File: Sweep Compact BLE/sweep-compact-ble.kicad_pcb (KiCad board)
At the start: 2 copper layers, 108.1 x 86.7 mm, 20 parts, among them SW10 SW_PUSH, SW11 SW_PUSH, SW12 SW_PUSH, SW14 SW_PUSH, SW15 SW_PUSH, SW16 SW_PUSH, SW17 SW_PUSH, SW18 SW_PUSH, SW2 SW_PUSH, SW20 SW_PUSH, SW21 SW_PUSH, SW3 SW_PUSH, SW4 SW_PUSH, SW5 SW_PUSH, SW6 SW_PUSH, SW8 SW_PUSH, SW9 SW_PUSH, U1 ProMicro

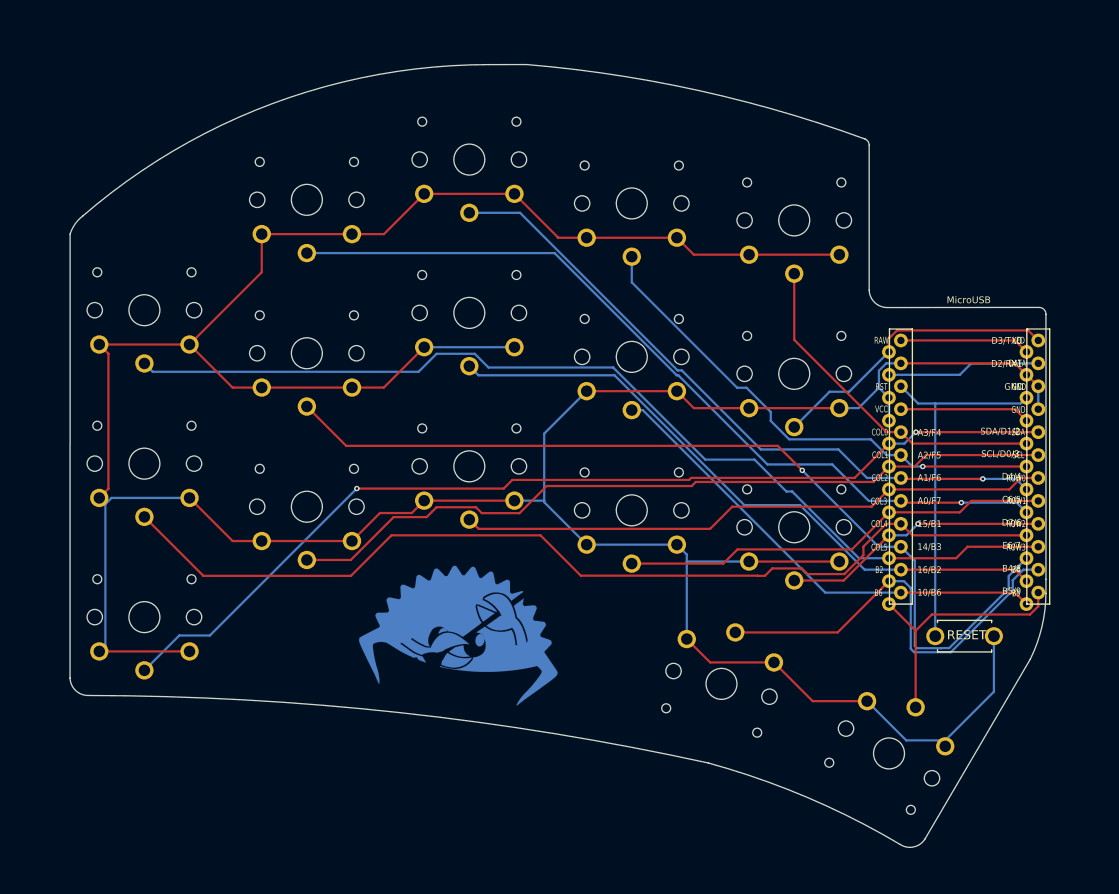
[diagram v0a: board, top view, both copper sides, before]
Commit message: superflous routing.
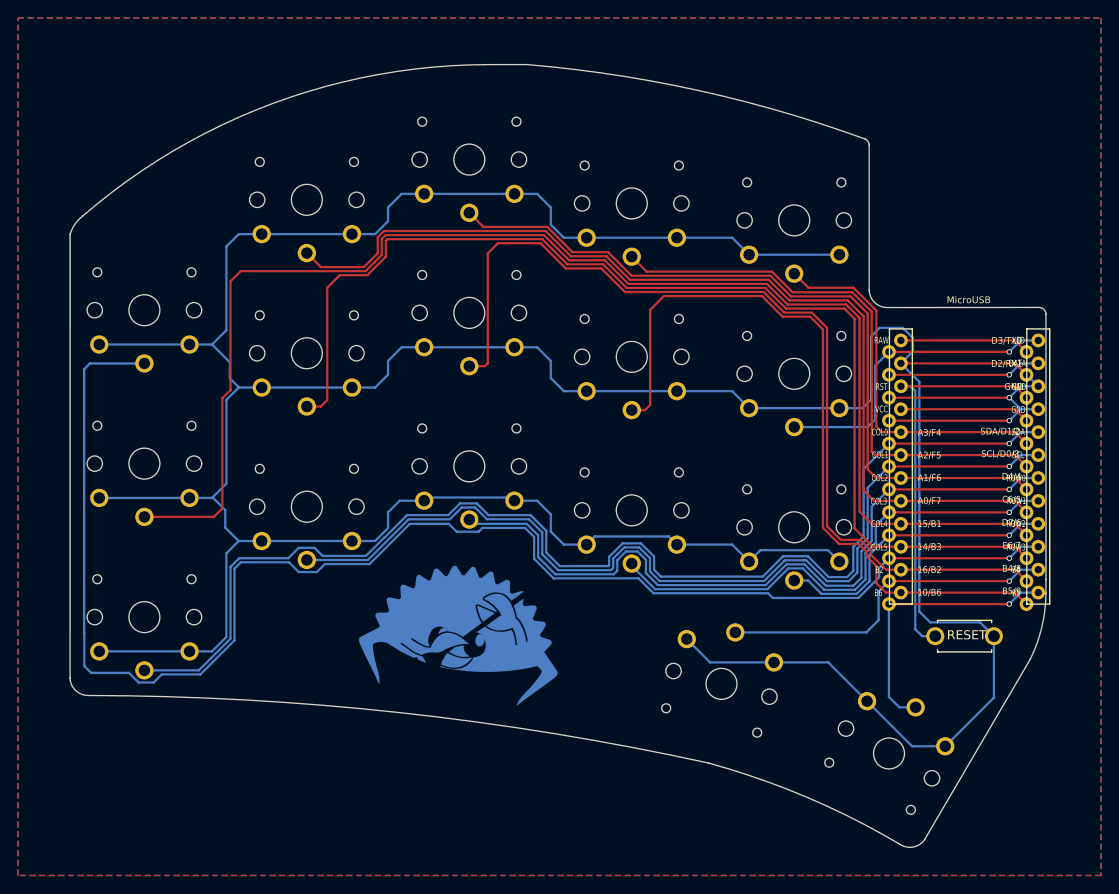
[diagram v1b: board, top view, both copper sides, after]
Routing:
- net GND: track 400.3 -> 469.4 mm, vias 0 -> 2
- net row3: track 110.2 -> 167.2 mm, vias 0 -> 1
- net col4: track 108.1 -> 152.3 mm
- net Net-(U1-Pad14): track 71.6 -> 103.2 mm
- net Net-(U1-Pad13): track 52.6 -> 83.5 mm
- net SDA: track 110.0 -> 134.9 mm, vias 2 -> 1
- net col5: track 101.3 -> 124.0 mm, vias 1 -> 0
- net SCL: track 86.4 -> 104.3 mm, vias 0 -> 1
- net row0: track 65.8 -> 81.9 mm, vias 0 -> 1
- net col3: track 91.6 -> 107.3 mm, vias 1 -> 0
- net col2: track 74.4 -> 84.5 mm, vias 1 -> 0
- net Net-(U1-Pad11): track 47.6 -> 38.3 mm, vias 0 -> 1
- net row1: track 47.9 -> 55.2 mm, vias 0 -> 1
- net col1: track 55.6 -> 62.4 mm, vias 1 -> 0
- net reset: track 40.7 -> 45.2 mm
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- added copper zone on B.Cu, net (none)
- added copper zone on F.Cu, net (none)
